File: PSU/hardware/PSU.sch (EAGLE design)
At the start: 202 parts, among them J1 SWD, J2 UART, Q1 PMOS-DPAK, Q10 PMOS-SOT23, Q11 NPN, Q2 PMOS-SOT23, Q3 NPN, Q4 PMOS-SOT23, Q5 NMOS-SOT23, Q6 PMOS-DPAK, Q7 PMOS-SOT23, Q8 NMOS-SOT23, Q9 PMOS-DPAK, U1 LM2576, U10 4069, U11 LTV-247, U12 74HC08, U13 STM8S003K3T6C, U14 74HC08, U15 4051, U16 358, U17 358, U18 74HC32, U2 MT3608, U3 7805, U4 324, U5 MC34063, U6 MT3608, U7 LM2576, U8 MC34063, U9 TP4056

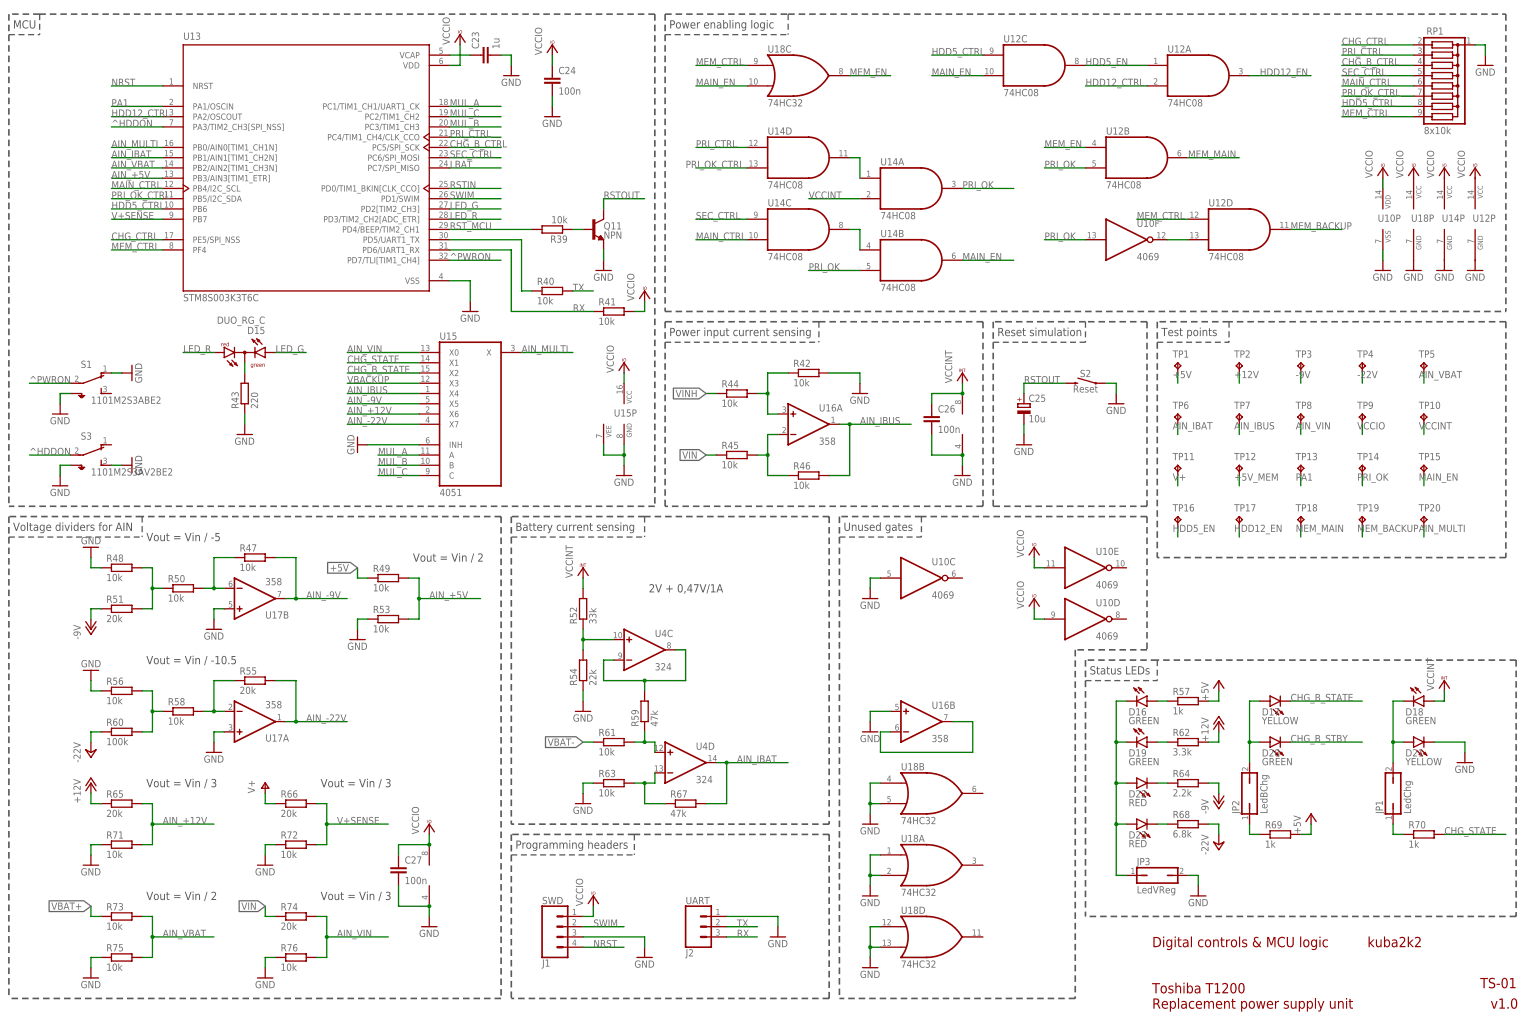
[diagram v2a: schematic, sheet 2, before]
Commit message: [HW/PSU] Fix LM2576 enable signals level
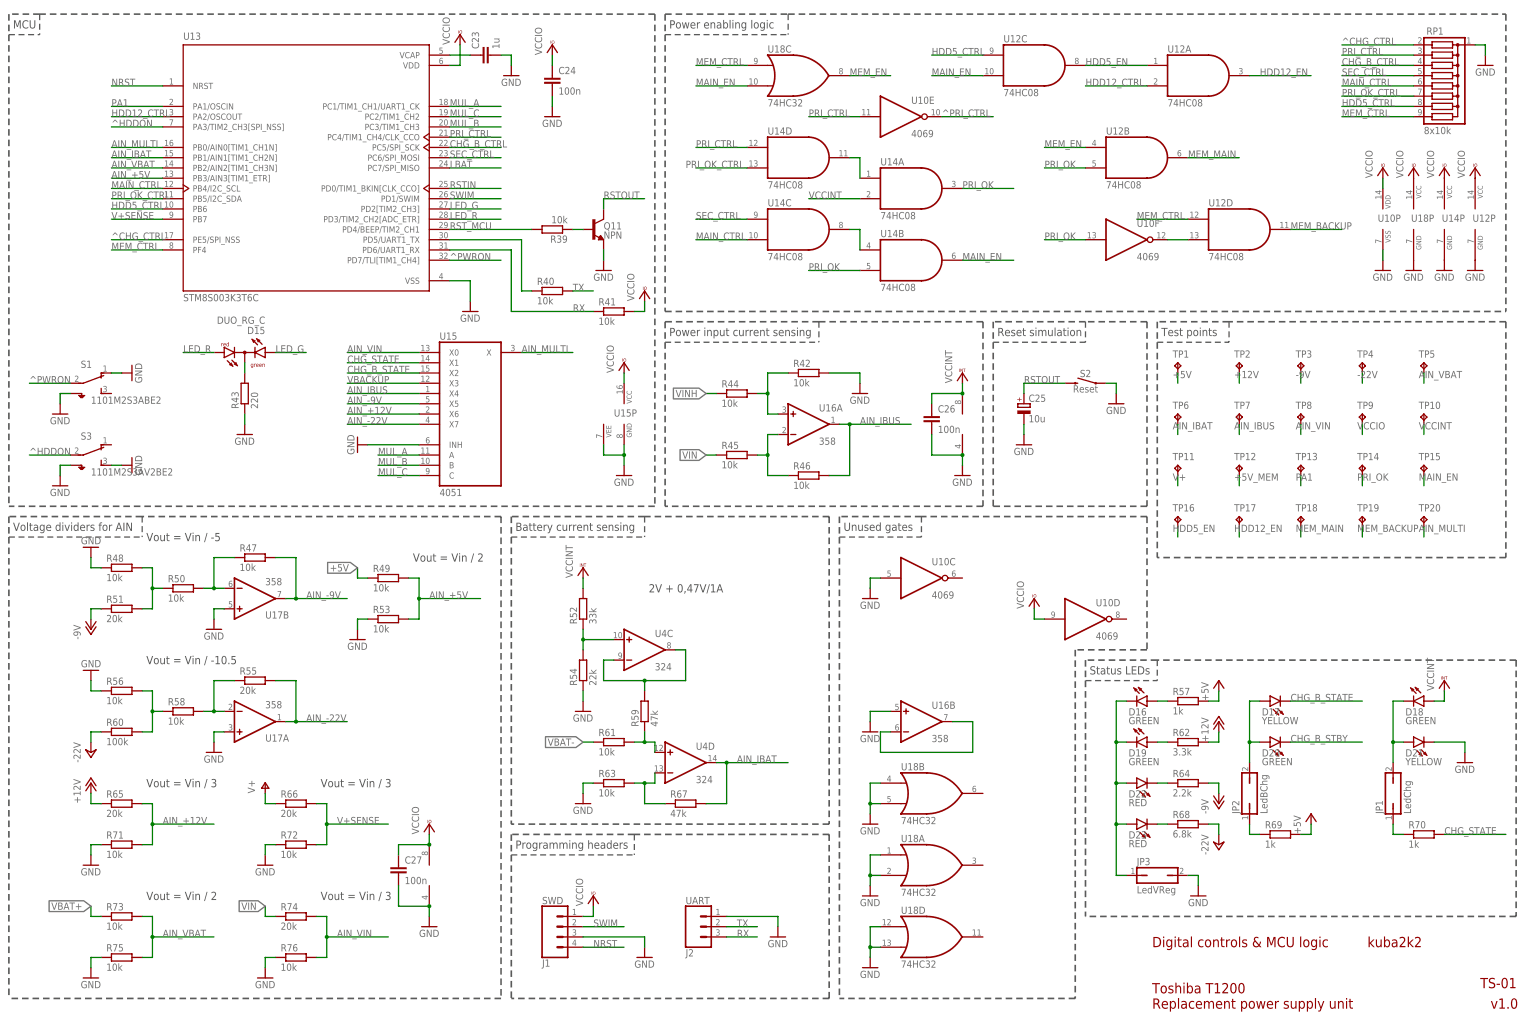
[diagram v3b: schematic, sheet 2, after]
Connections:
- net CHG_CTRL renamed ^CHG_CTRL
- new net ^PRI_CTRL: U1.EN, U10E.O
- net PRI_CTRL: now also U10E.I; no longer U1.EN
- net VCCIO: no longer U10E.I
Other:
- moved on the sheet: U10E
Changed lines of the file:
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@@
 <part name="R19" library="rcl" library_urn="urn:adsk.eagle:library:334" deviceset="R-EU_" device="0411/15" package3d_urn="urn:adsk.eagle:package:23568/2" value="0.1"/>
 <part name="VCC18" library="supply1" library_urn="urn:adsk.eagle:library:371" deviceset="VCCINT" device=""/>
-<part name="VCC19" library="supply1" library_urn="urn:adsk.eagle:library:371" deviceset="VCCIO" device=""/>
 <part name="VCC20" library="supply1" library_urn="urn:adsk.eagle:library:371" deviceset="VCCIO" device=""/>
 <part name="TP13" library="testpad" library_urn="urn:adsk.eagle:library:385" deviceset="TP" device="B1,27" package3d_urn="urn:adsk.eagle:package:27944/2"/>
@@
 </segment>
 </net>
-<net name="CHG_CTRL" class="1">
+<net name="^CHG_CTRL" class="1">
 <segment>
 <pinref part="U7" gate="NC1" pin="EN"/>
@@
 </segment>
 </net>
-<net name="PRI_CTRL" class="1">
-<segment>
-<pinref part="U1" gate="NC1" pin="EN"/>
-<wire x1="195.58" y1="228.6" x2="185.42" y2="228.6" width="0.1524" layer="91"/>
-<label x="185.42" y="228.6" size="1.778" layer="95"/>
-</segment>
-</net>
 <net name="FULL_VAL" class="1">
 <segment>
@@
 </segment>
 </net>
+<net name="^PRI_CTRL" class="1">
+<segment>
+<pinref part="U1" gate="NC1" pin="EN"/>
+<wire x1="195.58" y1="228.6" x2="185.42" y2="228.6" width="0.1524" layer="91"/>
+<label x="185.42" y="228.6" size="1.778" layer="95"/>
+</segment>
+</net>
 </nets>
 </sheet>
@@
 <attribute name="VALUE" x="241.3" y="160.02" size="1.778" layer="96" rot="R90"/>
 </instance>
-<instance part="U10" gate="E" x="274.32" y="114.3" smashed="yes">
-<attribute name="NAME" x="276.86" y="117.475" size="1.778" layer="95"/>
-<attribute name="VALUE" x="276.86" y="109.22" size="1.778" layer="96"/>
+<instance part="U10" gate="E" x="228.6" y="226.06" smashed="yes">
+<attribute name="NAME" x="231.14" y="229.235" size="1.778" layer="95"/>
+<attribute name="VALUE" x="231.14" y="220.98" size="1.778" layer="96"/>
 </instance>
 <instance part="U10" gate="C" x="233.68" y="111.76" smashed="yes">
@@
 <attribute name="VALUE" x="276.86" y="96.52" size="1.778" layer="96"/>
 </instance>
-<instance part="VCC19" gate="G$1" x="261.62" y="119.38" smashed="yes">
-<attribute name="VALUE" x="259.08" y="116.84" size="1.778" layer="96" rot="R90"/>
-</instance>
 <instance part="VCC20" gate="G$1" x="261.62" y="106.68" smashed="yes">
 <attribute name="VALUE" x="259.08" y="104.14" size="1.778" layer="96" rot="R90"/>
@@
 </segment>
 <segment>
-<pinref part="U10" gate="E" pin="I"/>
-<wire x1="264.16" y1="114.3" x2="261.62" y2="114.3" width="0.1524" layer="91"/>
-<wire x1="261.62" y1="114.3" x2="261.62" y2="116.84" width="0.1524" layer="91"/>
-<pinref part="VCC19" gate="G$1" pin="VCCIO"/>
-</segment>
-<segment>
 <pinref part="U10" gate="D" pin="I"/>
 <wire x1="264.16" y1="101.6" x2="261.62" y2="101.6" width="0.1524" layer="91"/>
@@
 </segment>
 </net>
-<net name="PRI_CTRL" class="1">
+<net name="^PRI_CTRL" class="1">
 <segment>
-<label x="177.8" y="218.44" size="1.778" layer="95"/>
-<pinref part="U14" gate="D" pin="I0"/>
-<wire x1="190.5" y1="218.44" x2="177.8" y2="218.44" width="0.1524" layer="91"/>
-</segment>
-<segment>
-<pinref part="U13" gate="G$1" pin="PC4/TIM1_CH4/CLK_CCO"/>
-<wire x1="116.84" y1="220.98" x2="129.54" y2="220.98" width="0.1524" layer="91"/>
-<label x="116.84" y="220.98" size="1.778" layer="95"/>
-</segment>
-<segment>
-<pinref part="RP1" gate="G$1" pin="2"/>
-<wire x1="337.82" y1="241.3" x2="355.6" y2="241.3" width="0.1524" layer="91"/>
-<label x="337.82" y="241.3" size="1.778" layer="95"/>
+<pinref part="U10" gate="E" pin="O"/>
+<wire x1="238.76" y1="226.06" x2="251.46" y2="226.06" width="0.1524" layer="91"/>
+<label x="238.76" y="226.06" size="1.778" layer="95"/>
 </segment>
 </net>
@@
 </segment>
 </net>
-<net name="CHG_CTRL" class="1">
+<net name="^CHG_CTRL" class="1">
 <segment>
 <pinref part="RP1" gate="G$1" pin="1"/>
@@
 </segment>
 </net>
+<net name="PRI_CTRL" class="1">
+<segment>
+<label x="177.8" y="218.44" size="1.778" layer="95"/>
+<pinref part="U14" gate="D" pin="I0"/>
+<wire x1="190.5" y1="218.44" x2="177.8" y2="218.44" width="0.1524" layer="91"/>
+</segment>
+<segment>
+<pinref part="U10" gate="E" pin="I"/>
+<wire x1="218.44" y1="226.06" x2="205.74" y2="226.06" width="0.1524" layer="91"/>
+<label x="205.74" y="226.06" size="1.778" layer="95"/>
+</segment>
+<segment>
+<pinref part="U13" gate="G$1" pin="PC4/TIM1_CH4/CLK_CCO"/>
+<wire x1="116.84" y1="220.98" x2="129.54" y2="220.98" width="0.1524" layer="91"/>
+<label x="116.84" y="220.98" size="1.778" layer="95"/>
+</segment>
+<segment>
+<pinref part="RP1" gate="G$1" pin="2"/>
+<wire x1="337.82" y1="241.3" x2="355.6" y2="241.3" width="0.1524" layer="91"/>
+<label x="337.82" y="241.3" size="1.778" layer="95"/>
+</segment>
+</net>

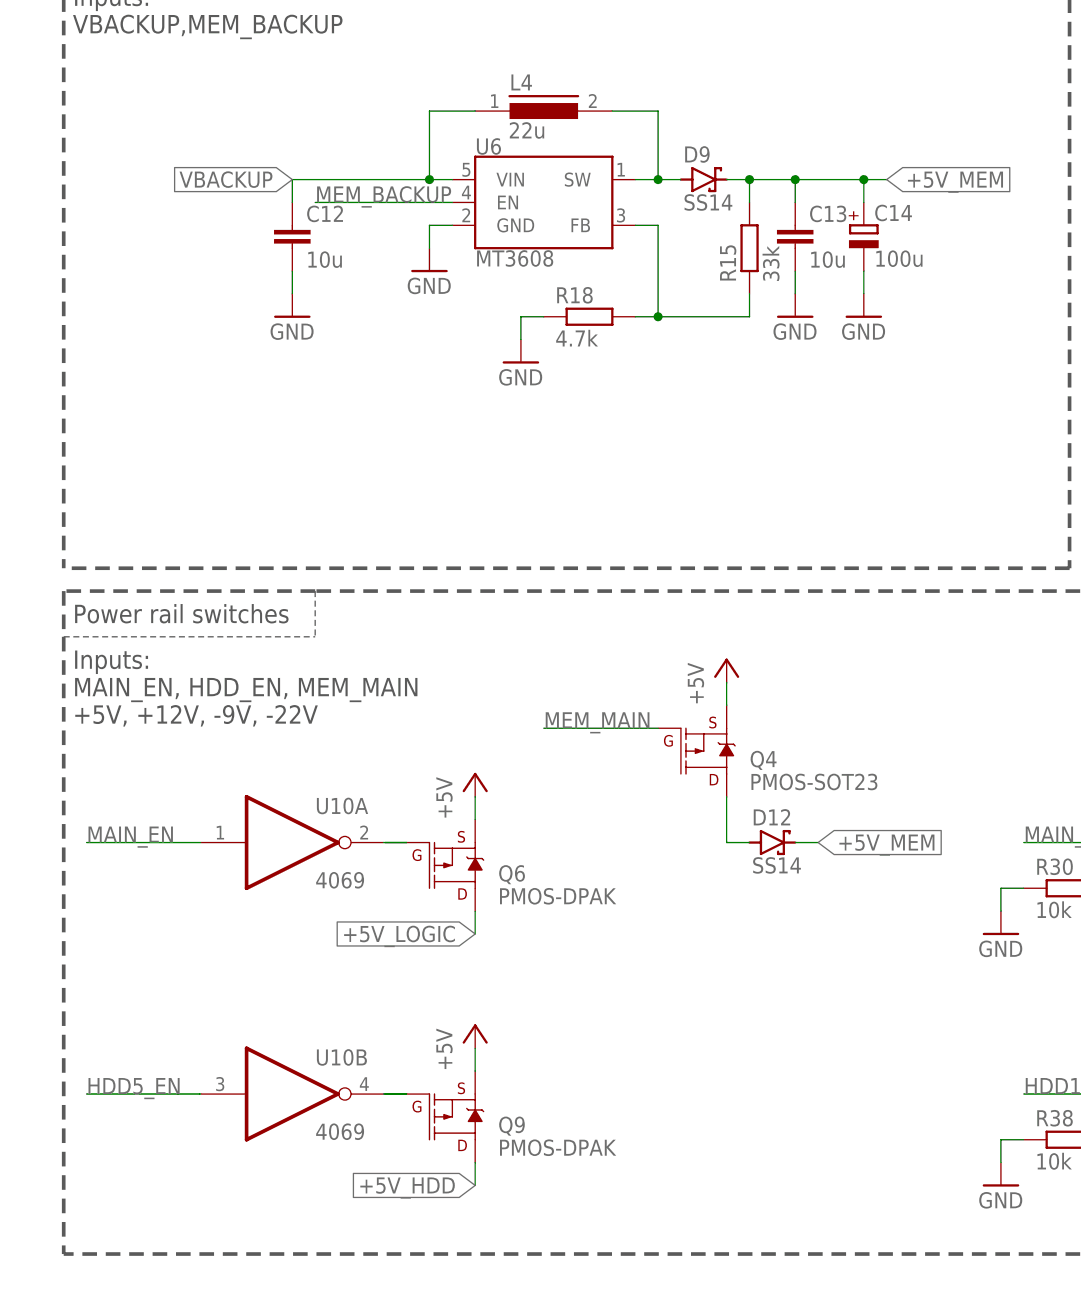
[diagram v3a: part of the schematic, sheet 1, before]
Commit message: [HW/PSU] Fix backup regulator enabling
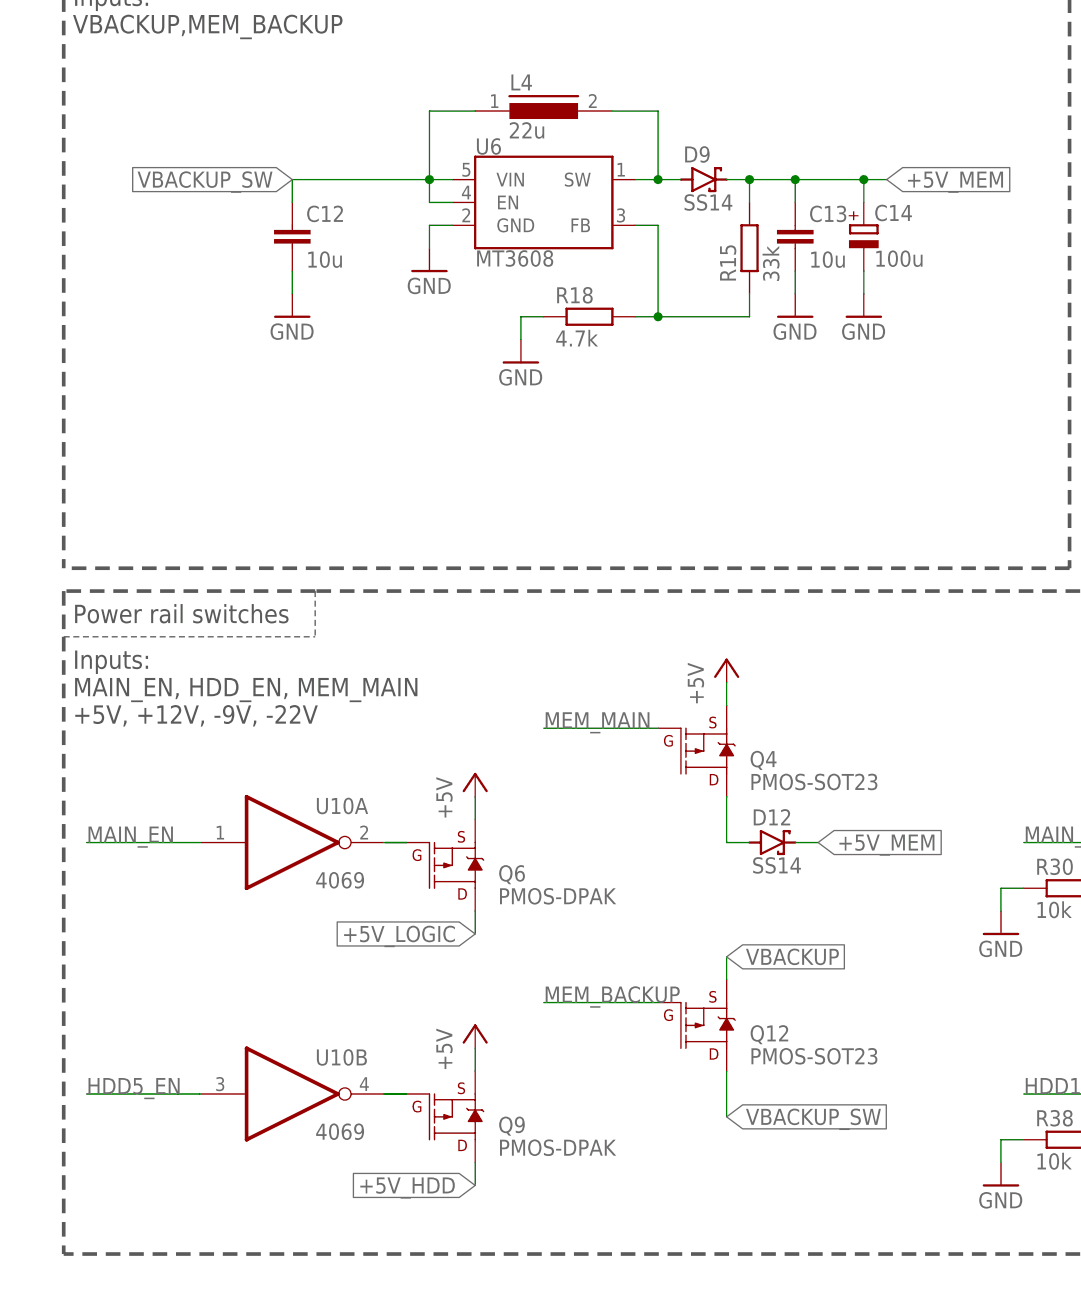
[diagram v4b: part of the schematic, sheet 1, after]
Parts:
- added Q12: PMOS-SOT23, SparkFun-DiscreteSemi:MOSFET_PCH-IRLML2244
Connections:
- new net VBACKUP_SW: C12.1, L4.1, Q12.D, U6.EN, U6.VIN
- net MEM_BACKUP: now also Q12.G; no longer U6.EN
- net VBACKUP: now also Q12.S; no longer C12.1, L4.1, U6.VIN
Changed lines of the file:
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@@
 <part name="R32" library="rcl" library_urn="urn:adsk.eagle:library:334" deviceset="R-EU_" device="R1206" package3d_urn="urn:adsk.eagle:package:23540/2" value="0.4"/>
 <part name="TP17" library="testpad" library_urn="urn:adsk.eagle:library:385" deviceset="TP" device="B1,27" package3d_urn="urn:adsk.eagle:package:27944/2"/>
+<part name="Q12" library="SparkFun-DiscreteSemi" deviceset="MOSFET_PCH" device="-IRLML2244" value="PMOS-SOT23"/>
 </parts>
 <sheets>
@@
 <attribute name="VALUE" x="323.342" y="39.37" size="1.778" layer="96" rot="R90"/>
 </instance>
+<instance part="Q12" gate="G$1" x="78.74" y="33.02" smashed="yes" rot="MR180">
+<attribute name="NAME" x="83.82" y="33.02" size="1.778" layer="95" font="vector" rot="MR180"/>
+<attribute name="VALUE" x="83.82" y="30.48" size="1.778" layer="96" font="vector" rot="MR180"/>
+</instance>
 </instances>
 <busses>
@@
 </segment>
 <segment>
-<pinref part="U6" gate="G$1" pin="VIN"/>
-<wire x1="50.8" y1="127" x2="48.26" y2="127" width="0.1524" layer="91"/>
-<pinref part="C12" gate="G$1" pin="1"/>
-<wire x1="48.26" y1="127" x2="33.02" y2="127" width="0.1524" layer="91"/>
-<wire x1="53.34" y1="134.62" x2="48.26" y2="134.62" width="0.1524" layer="91"/>
-<wire x1="48.26" y1="134.62" x2="48.26" y2="127" width="0.1524" layer="91"/>
-<junction x="48.26" y="127"/>
-<wire x1="33.02" y1="127" x2="33.02" y2="124.46" width="0.1524" layer="91"/>
-<label x="33.02" y="127" size="1.778" layer="95" rot="R180" xref="yes"/>
-<pinref part="L4" gate="G$1" pin="1"/>
-</segment>
-<segment>
 <pinref part="D4" gate="G$1" pin="A"/>
 <wire x1="172.72" y1="180.34" x2="170.18" y2="180.34" width="0.1524" layer="91"/>
 <label x="170.18" y="180.34" size="1.778" layer="95" rot="R180" xref="yes"/>
+</segment>
+<segment>
+<pinref part="Q12" gate="G$1" pin="S"/>
+<wire x1="81.28" y1="38.1" x2="81.28" y2="40.64" width="0.1524" layer="91"/>
+<label x="81.28" y="40.64" size="1.778" layer="95" xref="yes"/>
 </segment>
 </net>
@@
 <net name="MEM_BACKUP" class="1">
 <segment>
-<pinref part="U6" gate="G$1" pin="EN"/>
-<wire x1="50.8" y1="124.46" x2="35.56" y2="124.46" width="0.1524" layer="91"/>
-<label x="35.56" y="124.46" size="1.778" layer="95"/>
+<wire x1="73.66" y1="35.56" x2="60.96" y2="35.56" width="0.1524" layer="91"/>
+<pinref part="Q12" gate="G$1" pin="G"/>
+<label x="60.96" y="35.56" size="1.778" layer="95"/>
 </segment>
 </net>
@@
 </segment>
 </net>
+<net name="VBACKUP_SW" class="2">
+<segment>
+<pinref part="Q12" gate="G$1" pin="D"/>
+<wire x1="81.28" y1="27.94" x2="81.28" y2="22.86" width="0.1524" layer="91"/>
+<label x="81.28" y="22.86" size="1.778" layer="95" xref="yes"/>
+</segment>
+<segment>
+<pinref part="U6" gate="G$1" pin="VIN"/>
+<wire x1="50.8" y1="127" x2="48.26" y2="127" width="0.1524" layer="91"/>
+<pinref part="C12" gate="G$1" pin="1"/>
+<wire x1="48.26" y1="127" x2="33.02" y2="127" width="0.1524" layer="91"/>
+<wire x1="53.34" y1="134.62" x2="48.26" y2="134.62" width="0.1524" layer="91"/>
+<wire x1="48.26" y1="134.62" x2="48.26" y2="127" width="0.1524" layer="91"/>
+<junction x="48.26" y="127"/>
+<wire x1="33.02" y1="127" x2="33.02" y2="124.46" width="0.1524" layer="91"/>
+<label x="33.02" y="127" size="1.778" layer="95" rot="R180" xref="yes"/>
+<pinref part="L4" gate="G$1" pin="1"/>
+<pinref part="U6" gate="G$1" pin="EN"/>
+<wire x1="50.8" y1="124.46" x2="48.26" y2="124.46" width="0.1524" layer="91"/>
+<wire x1="48.26" y1="124.46" x2="48.26" y2="127" width="0.1524" layer="91"/>
+</segment>
+</net>
